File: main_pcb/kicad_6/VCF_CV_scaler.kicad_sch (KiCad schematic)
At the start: 15 parts, among them J1301 aux_VCF_FM_in, U5 TL072

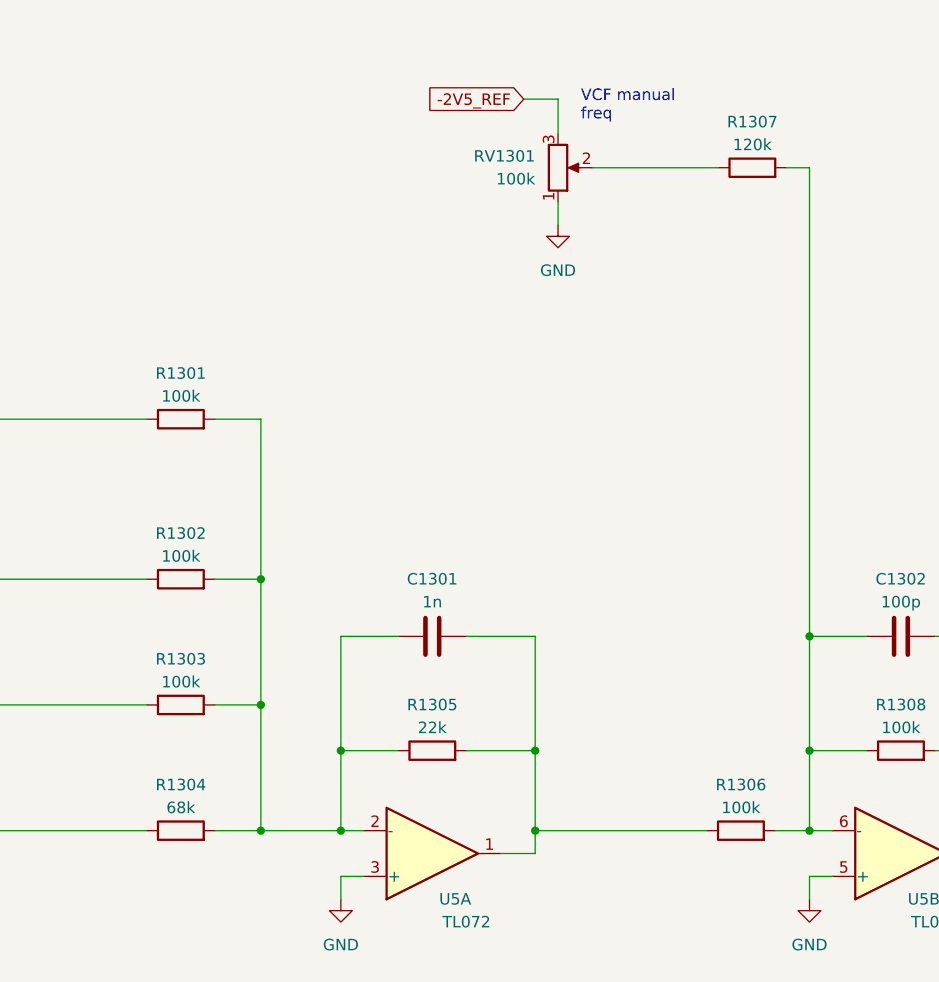
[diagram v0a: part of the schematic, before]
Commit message: Update rev 0.1, fix VCA tails, add local 2v5 regs, change some pot footprints
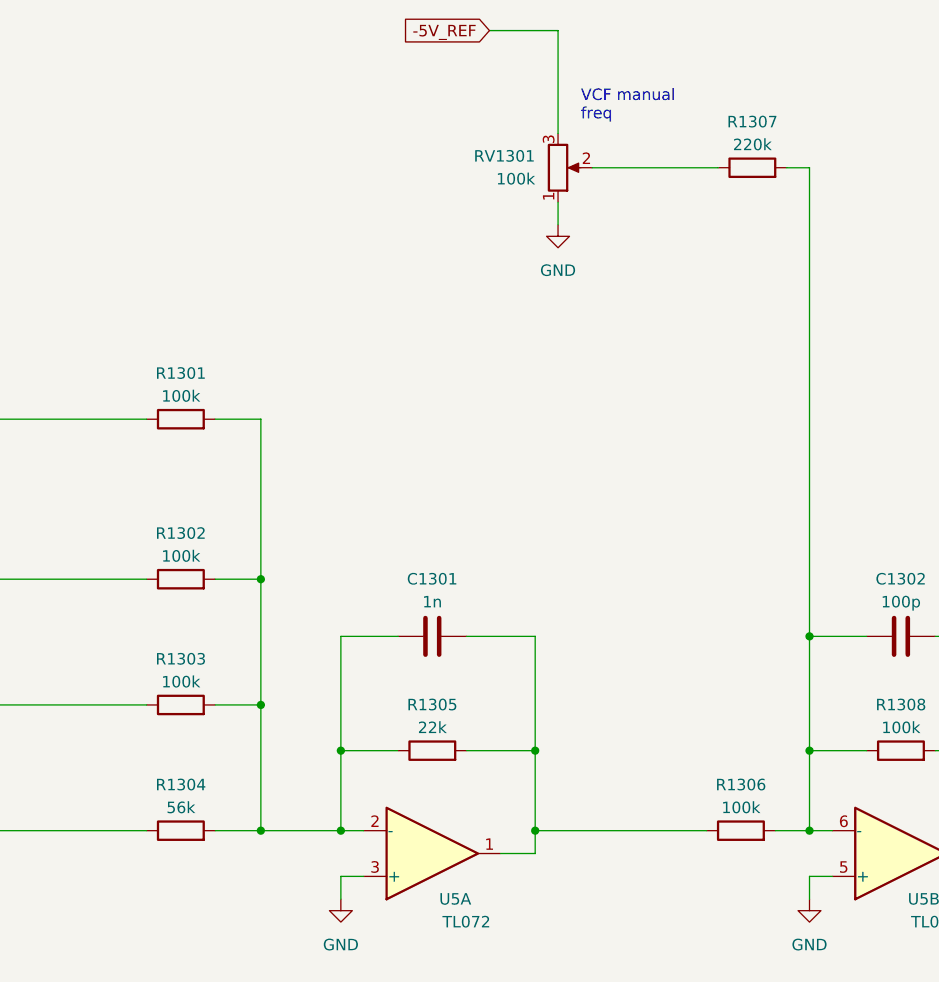
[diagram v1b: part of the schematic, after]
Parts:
- J1301: now left out of the parts list
- R1304: value 68k -> 56k
- R1307: value 120k -> 220k
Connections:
- net -2V5_REF renamed -5V_REF
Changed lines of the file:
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@@
   (title_block
     (title "Micro-Pico Tiny Monosynth")
-    (date "2022-08-18")
+    (date "2022-08-28")
     (rev "0.1")
     (comment 1 "creativecommons.org/licences/by/4.0")
@@
     (stroke (width 0) (type default) (color 0 0 0 0))
   )
-  (wire (pts (xy 149.86 43.18) (xy 149.86 46.99))
-    (stroke (width 0) (type default) (color 0 0 0 0))
-  )
-  (wire (pts (xy 146.05 43.18) (xy 149.86 43.18))
+  (wire (pts (xy 149.86 35.56) (xy 149.86 46.99))
     (stroke (width 0) (type default) (color 0 0 0 0))
   )
@@
   )
   (wire (pts (xy 147.32 124.46) (xy 147.32 115.57))
+    (stroke (width 0) (type default) (color 0 0 0 0))
+  )
+  (wire (pts (xy 142.24 35.56) (xy 149.86 35.56))
     (stroke (width 0) (type default) (color 0 0 0 0))
   )
@@
     (effects (font (size 1.7 1.7)) (justify left bottom))
   )
-  (global_label "-2V5_REF" (shape input) (at 146.05 43.18 180) (fields_autoplaced)
+  (global_label "-5V_REF" (shape input) (at 142.24 35.56 180) (fields_autoplaced)
     (effects (font (size 1.27 1.27)) (justify right))
-    (property "Intersheet References" "${INTERSHEET_REFS}" (id 0) (at 134.0817 43.2594 0)
+    (property "Intersheet References" "${INTERSHEET_REFS}" (id 0) (at 131.4812 35.6394 0)
       (effects (font (size 1.27 1.27)) (justify right) hide)
     )
@@
     (in_bom yes) (on_board yes)
     (property "Reference" "R1307" (id 0) (at 171.45 45.72 90))
-    (property "Value" "120k" (id 1) (at 171.45 48.26 90))
+    (property "Value" "220k" (id 1) (at 171.45 48.26 90))
     (property "Footprint" "Resistor_SMD:R_0603_1608Metric" (id 2) (at 171.45 52.578 90)
       (effects (font (size 1.27 1.27)) hide)
@@
     (in_bom yes) (on_board yes)
     (property "Reference" "R1304" (id 0) (at 107.95 119.38 90))
-    (property "Value" "68k" (id 1) (at 107.95 121.92 90))
+    (property "Value" "56k" (id 1) (at 107.95 121.92 90))
     (property "Footprint" "Resistor_SMD:R_0603_1608Metric" (id 2) (at 107.95 126.238 90)
       (effects (font (size 1.27 1.27)) hide)
@@
   )
   (symbol (lib_id "Connector_Generic:Conn_01x01") (at 76.2 78.74 0) (mirror y) (unit 1)
-    (in_bom yes) (on_board yes) (fields_autoplaced)
+    (in_bom no) (on_board yes) (fields_autoplaced)
     (property "Reference" "J1301" (id 0) (at 76.2 72.39 0))
     (property "Value" "aux_VCF_FM_in" (id 1) (at 76.2 74.93 0))
